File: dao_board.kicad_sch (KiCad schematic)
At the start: 40 parts, among them J1 DISH_LED, J10 KEY6, J11 KEY7, J12 START, J13 SELECT, J14 DISH_SENSOR, J2 USB_C, J3 SWD, J4 GPIO_EXPANSION, J5 KEY1, J6 KEY2, J7 KEY3, J8 KEY4, J9 KEY5, SW1 HX 3x4x2-2P-1.6N, SW2 SW_Push, U1 MDBT50Q-1MV2

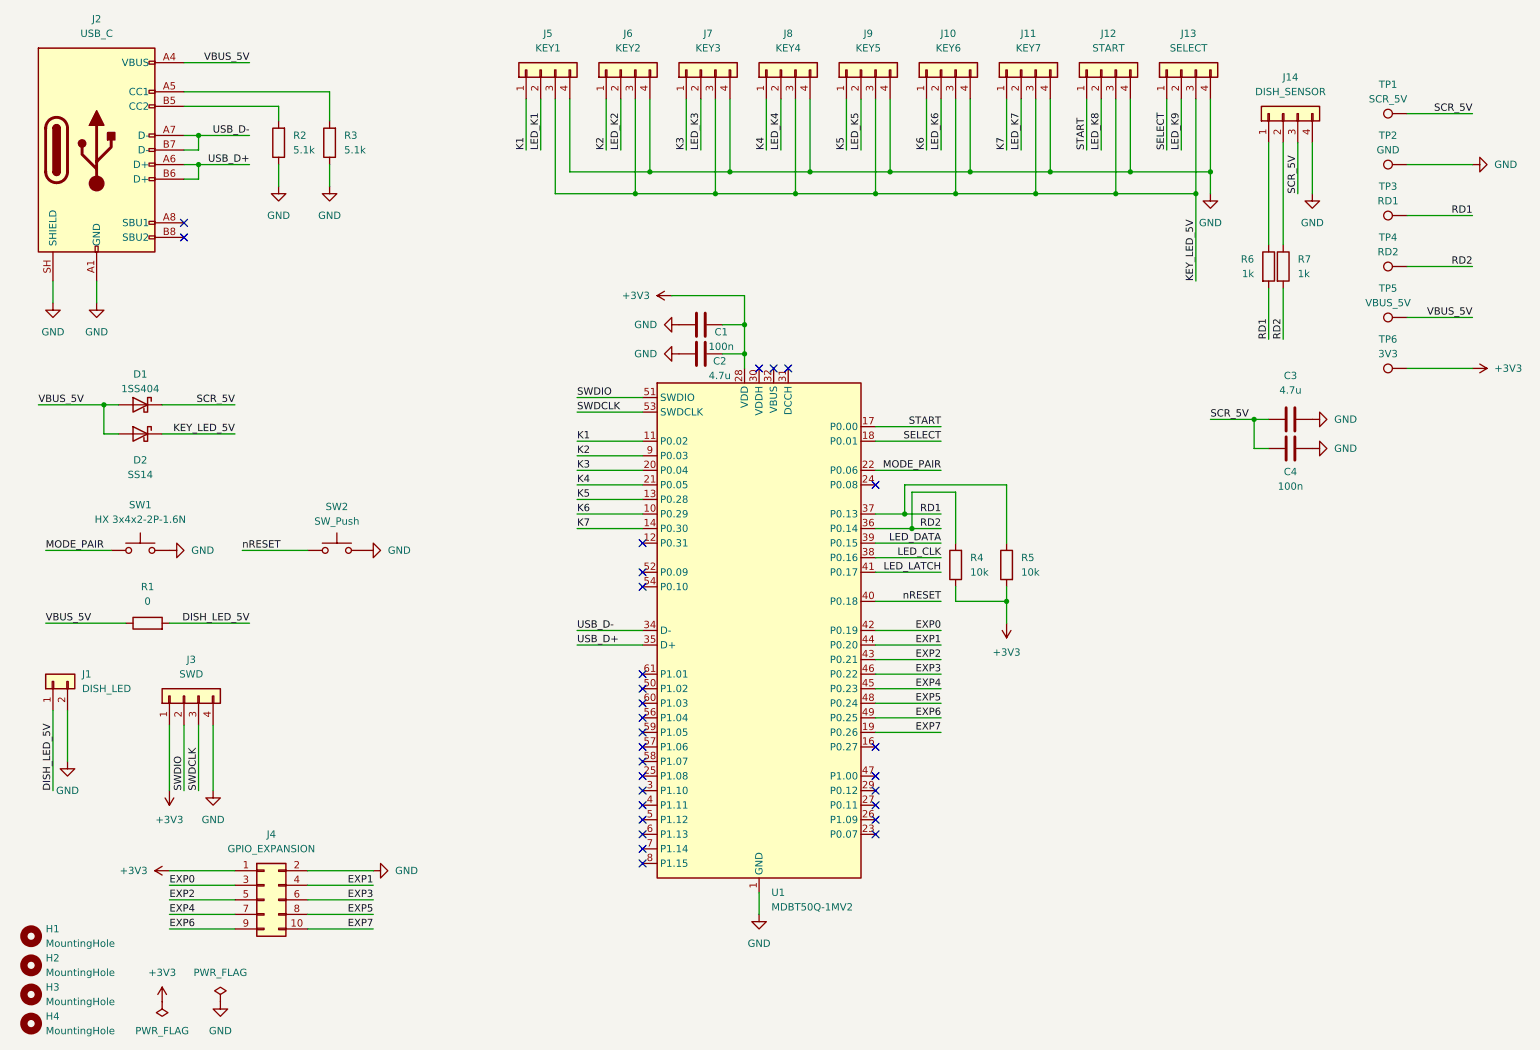
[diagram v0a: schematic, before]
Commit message: LEDドライバーの選定、データを引っ張ってきて配置だけした
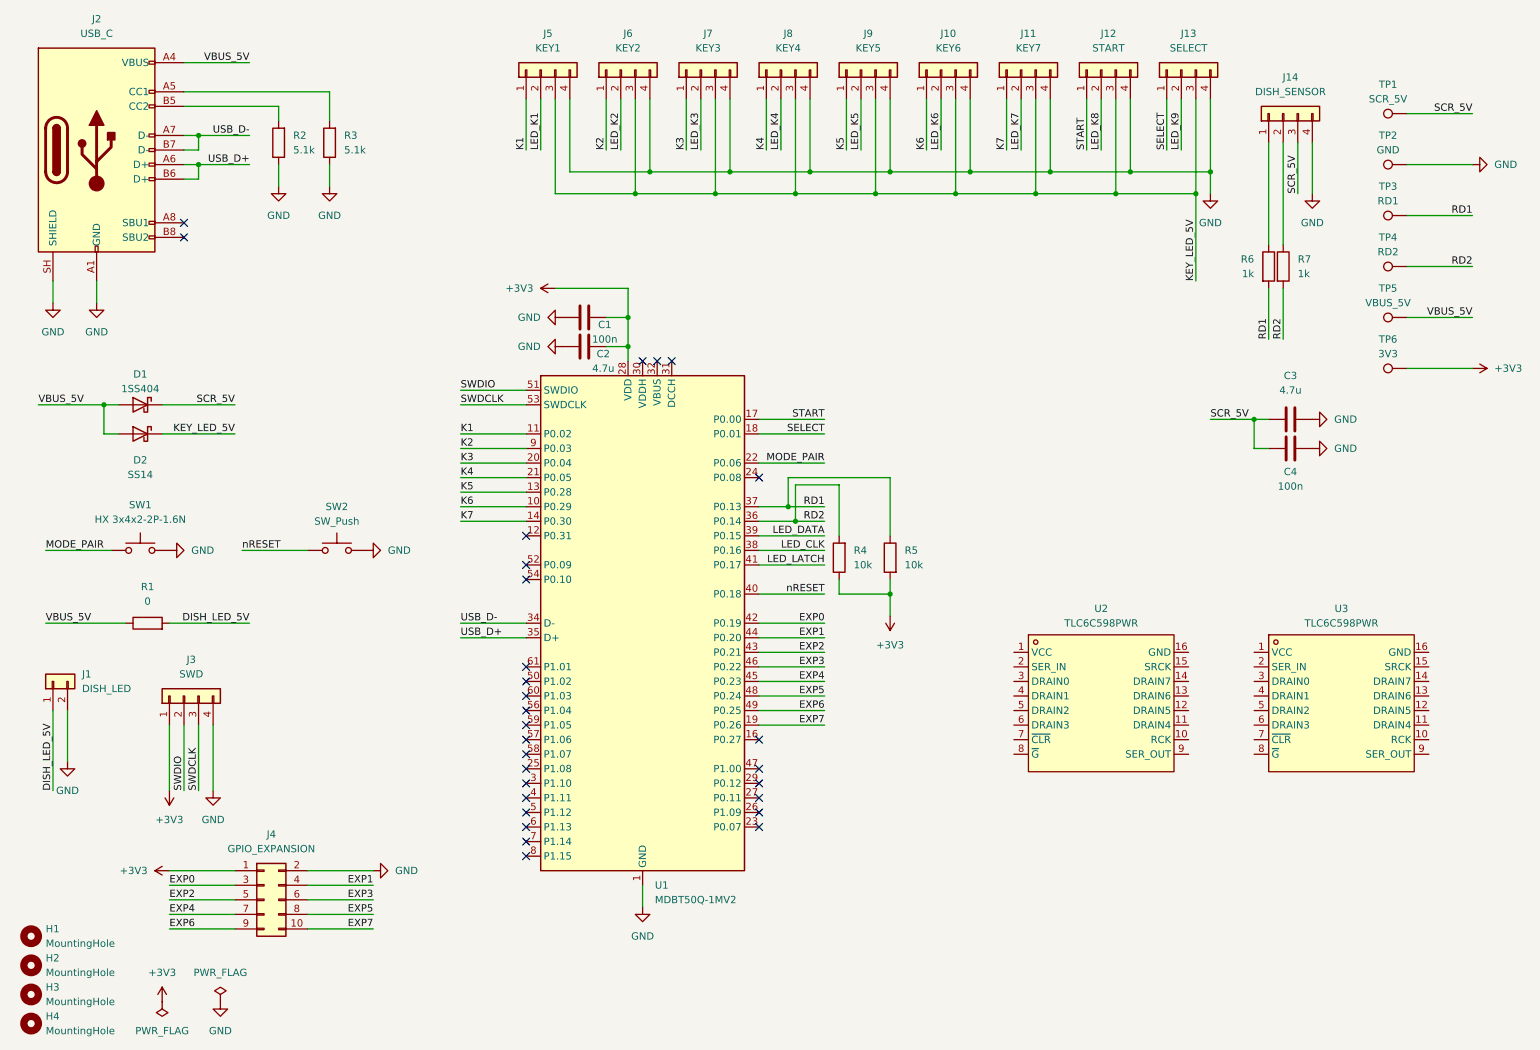
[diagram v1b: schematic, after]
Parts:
- added U2, U3: TLC6C598PWR, c2863406:TSSOP-16_L5.0-W4.4-P0.65-LS6.4-BL, symbol c2863406:TLC6C598PWR
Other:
- moved on the sheet: C1, C2, R4, R5, U1

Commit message: LEDドライバーの電源周りだけ配線
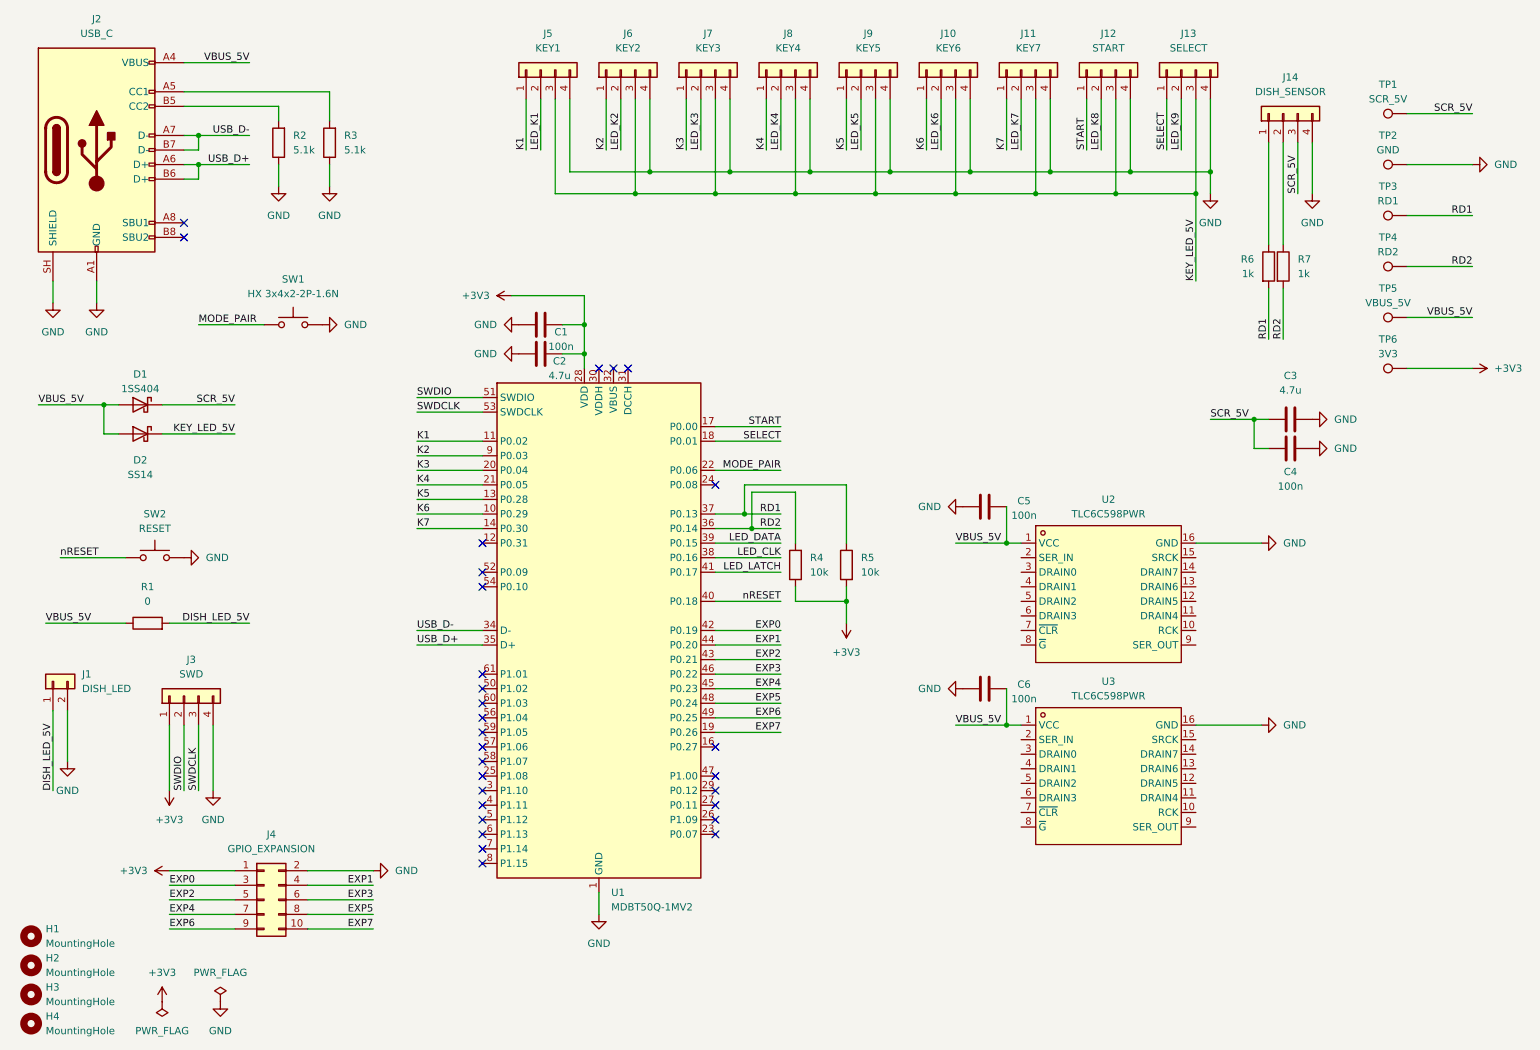
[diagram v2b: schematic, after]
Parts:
- added C5, C6: 100n, Library:C_0402_1005Metric, symbol Device:C
- SW2: value SW_Push -> RESET
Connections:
- net GND: now also U2.16 (GND), U3.16 (GND), C5.1, C6.1
- net VBUS_5V: now also U2.1 (VCC), U3.1 (VCC), C5.2, C6.2
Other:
- moved on the sheet: C1, C2, R4, R5, SW1, SW2, U1, U2, U3

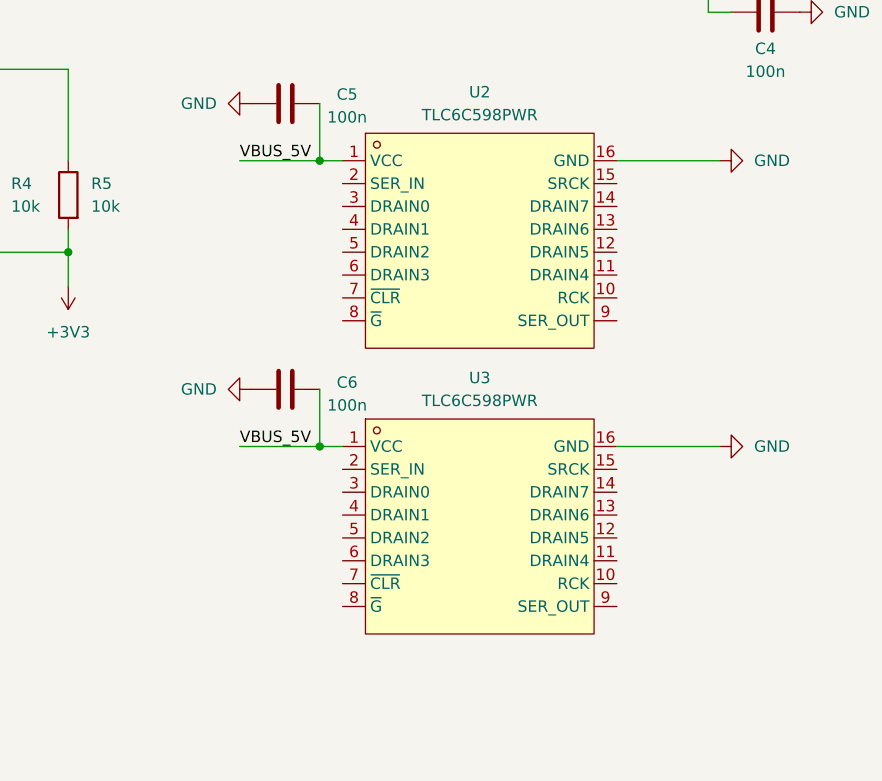
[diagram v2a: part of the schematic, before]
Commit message: LEDとドライバーの接続、未使用ピンを未接続としてマーク
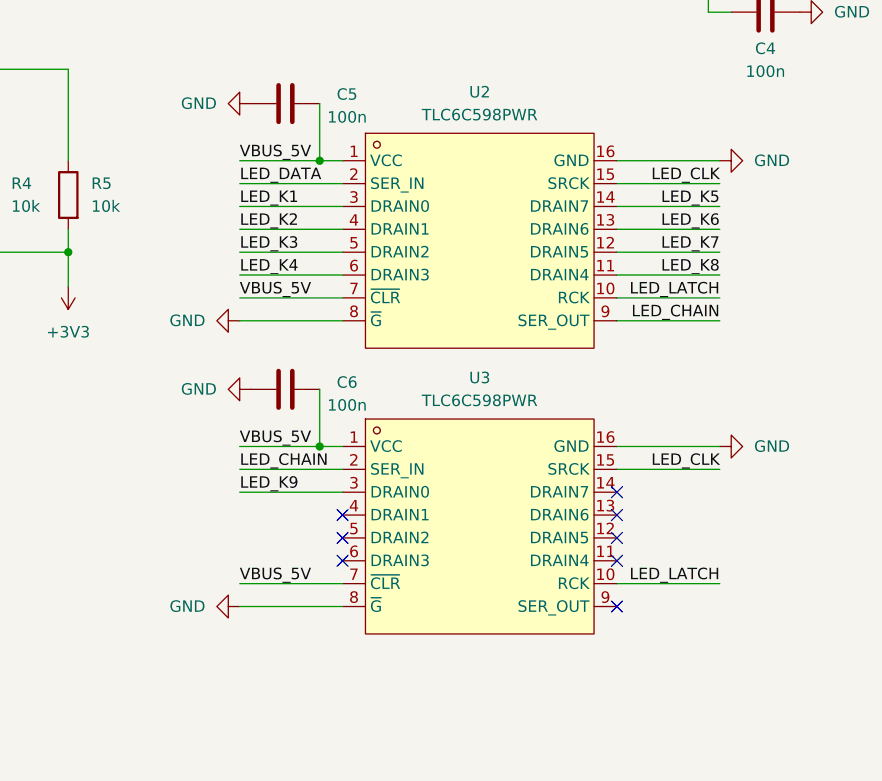
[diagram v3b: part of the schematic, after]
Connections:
- net GND: now also U2.8 (~{G}), U3.8 (~{G})
- net LED_CLK: now also U2.15 (SRCK), U3.15 (SRCK)
- net LED_DATA: now also U2.2 (SER_IN)
- net LED_K1: now also U2.3 (DRAIN0)
- net LED_K2: now also U2.4 (DRAIN1)
- net LED_K3: now also U2.5 (DRAIN2)
- net LED_K4: now also U2.6 (DRAIN3)
- net LED_K5: now also U2.14 (DRAIN7)
- net LED_K6: now also U2.13 (DRAIN6)
- net LED_K7: now also U2.12 (DRAIN5)
- net LED_K8: now also U2.11 (DRAIN4)
- net LED_K9: now also U3.3 (DRAIN0)
- net LED_LATCH: now also U2.10 (RCK), U3.10 (RCK)
- net VBUS_5V: now also U2.7 (~{CLR}), U3.7 (~{CLR})
- net LED_CHAIN: now reaches U2.9 (SER_OUT)
- net LED_CHAIN: now also U3.2 (SER_IN)
- no-connect marks 29 -> 37

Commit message: LEDとの接続ミスってたので修正、反時計回りになるの毎回忘れるんだが
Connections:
- net LED_K5: now also U2.11 (DRAIN4); no longer U2.14 (DRAIN7)
- net LED_K6: now also U2.12 (DRAIN5); no longer U2.13 (DRAIN6)
- net LED_K7: now also U2.13 (DRAIN6); no longer U2.12 (DRAIN5)
- net LED_K8: now also U2.14 (DRAIN7); no longer U2.11 (DRAIN4)

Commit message: 一旦の回路図完成、LEDドライバーのシンボルのピンが全て未指定だったので正しく変更した
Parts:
- U1: footprint c5118826:COMM-SMD_MDBT50Q-1MV2-1 -> RF_Module:Raytac_MDBT50Q
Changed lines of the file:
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@@
 	(wire
 		(pts
+			(xy 80.01 194.31) (xy 68.58 194.31)
+		)
+		(stroke
+			(width 0)
+			(type default)
+		)
+	)
+	(wire
+		(pts
 			(xy 137.16 129.54) (xy 148.59 129.54)
 		)
@@
 		)
 	)
+	(label "VBUS_5V"
+		(at 80.01 194.31 180)
+		(effects
+			(font
+				(size 1.27 1.27)
+			)
+			(justify right bottom)
+		)
+	)
 	(label "DISH_LED_5V"
 		(at 21.59 152.4 90)
@@
 			)
 		)
-		(property "Footprint" "c5118826:COMM-SMD_MDBT50Q-1MV2-1"
+		(property "Footprint" "RF_Module:Raytac_MDBT50Q"
 			(at 116.84 129.54 0)
 			(hide yes)
@@
 					(unit 1)
 				)
+			)
+		)
+	)
+	(symbol
+		(lib_id "power:PWR_FLAG")
+		(at 68.58 194.31 90)
+		(unit 1)
+		(body_style 1)
+		(exclude_from_sim no)
+		(in_bom yes)
+		(on_board yes)
+		(in_pos_files yes)
+		(dnp no)
+		(fields_autoplaced yes)
+		(property "Reference" "#FLG03"
+			(at 66.675 194.31 0)
+			(hide yes)
+			(show_name no)
+			(do_not_autoplace no)
+			(effects
+				(font
+					(size 1.27 1.27)
+				)
+			)
+		)
+		(property "Value" "PWR_FLAG"
+			(at 64.77 194.3099 90)
+			(show_name no)
+			(do_not_autoplace no)
+			(effects
+				(font
+					(size 1.27 1.27)
+				)
+				(justify left)
+			)
+		)
+		(property "Footprint" ""
+			(at 68.58 194.31 0)
+			(hide yes)
+			(show_name no)
+			(do_not_autoplace no)
+			(effects
+				(font
+					(size 1.27 1.27)
+				)
+			)
+		)
+		(property "Datasheet" ""
+			(at 68.58 194.31 0)
+			(hide yes)
+			(show_name no)
+			(do_not_autoplace no)
+			(effects
+				(font
+					(size 1.27 1.27)
+				)
+			)
+		)
+		(property "Description" "Special symbol for telling ERC where power comes from"
+			(at 68.58 194.31 0)
+			(hide yes)
+			(show_name no)
+			(do_not_autoplace no)
+			(effects
+				(font
+					(size 1.27 1.27)
+				)
+			)
+		)
+		(pin "1"
+		)
+		(instances
+			(project "dao_board"
+				(path "/88e2b3bc-f15b-46e0-bc23-bfcd5e24d1de"
+					(reference "#FLG03")
+					(unit 1)
+				)
